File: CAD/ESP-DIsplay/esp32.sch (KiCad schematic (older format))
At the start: 7 parts, among them U401 ESP32-WROOM-32

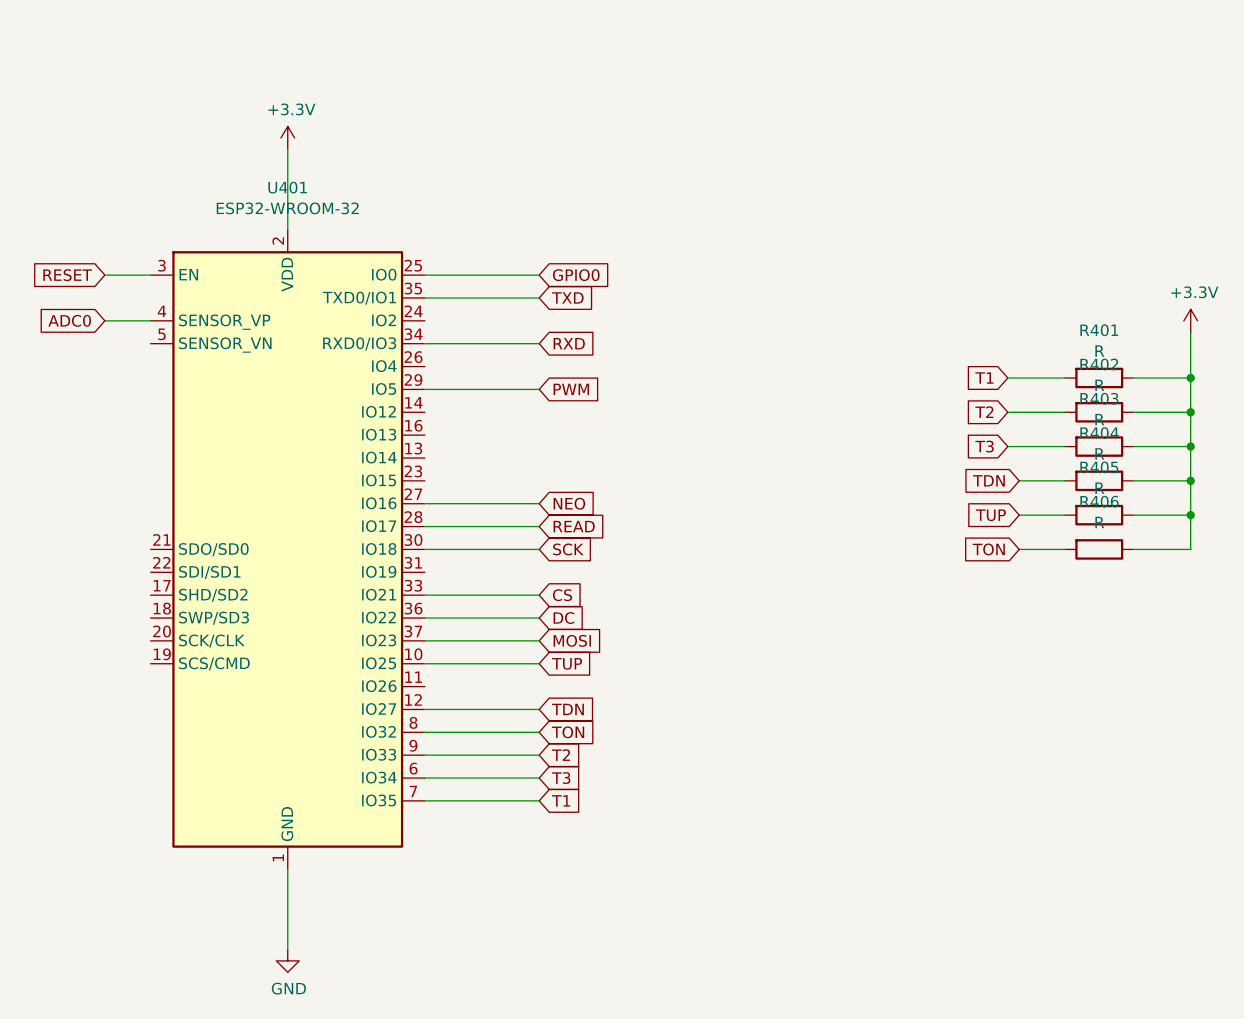
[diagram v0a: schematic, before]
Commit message: ESP Display v1
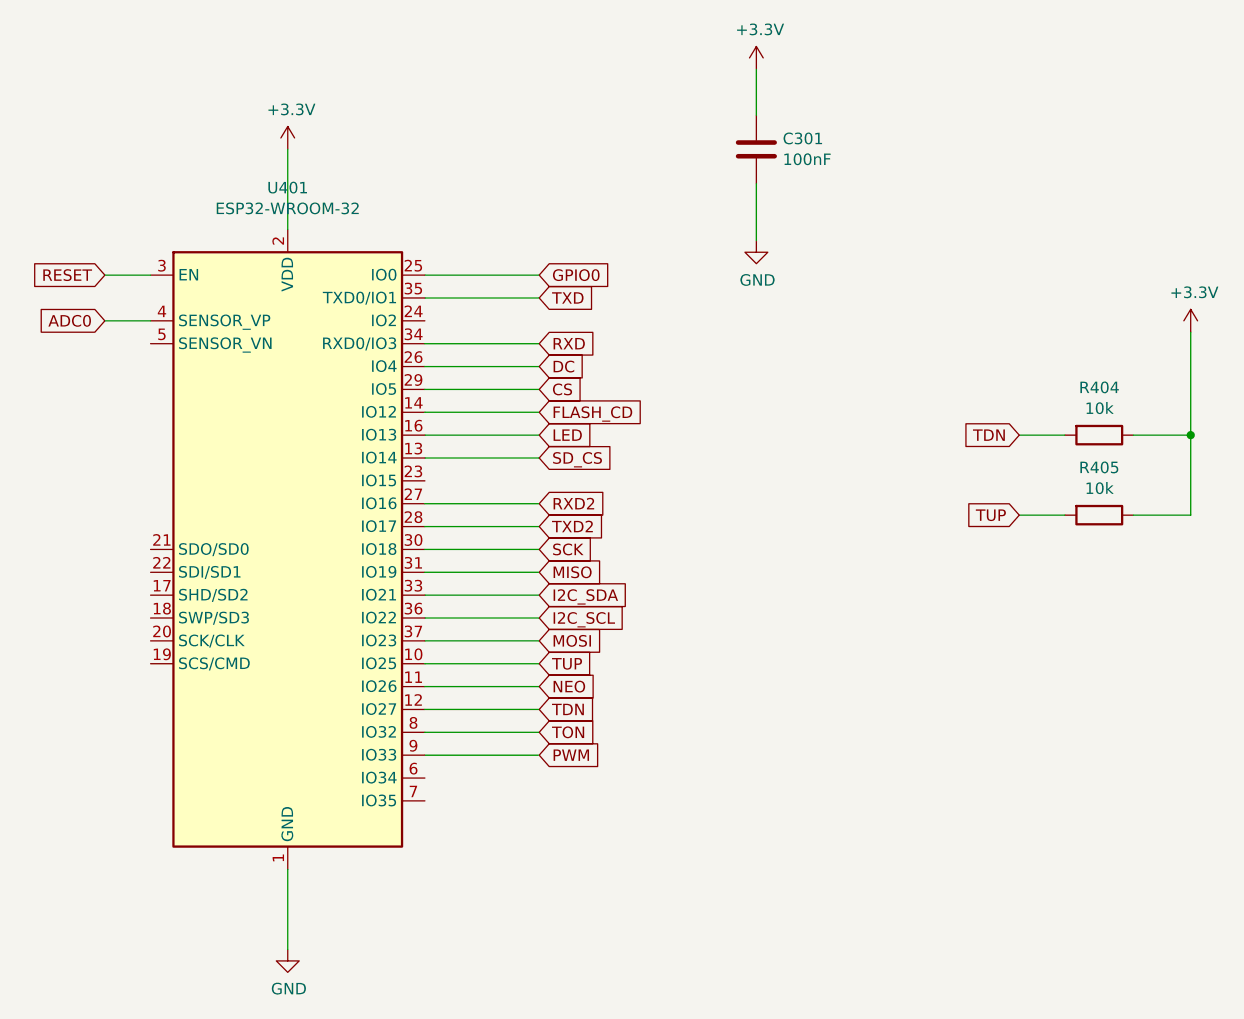
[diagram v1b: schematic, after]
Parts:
- removed R401, R402, R403, R406: R, Resistor_SMD:R_0805_2012Metric, symbol Device:R
- added C301: 100nF, Capacitor_SMD:C_1206_3216Metric, symbol Device:C
- R404, R405: value R -> 10k
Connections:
- net T2 is gone; now on net PWM: U401.9 (IO33)
- net +3V3: now also C301.1
- net CS: now also U401.29 (IO5); no longer U401.33 (IO21)
- net DC: now also U401.26 (IO4); no longer U401.36 (IO22)
- net GND: now also C301.2
- net NEO: now also U401.11 (IO26); no longer U401.27 (IO16)
- net PWM: no longer U401.29 (IO5)
- net SD_CS: now reaches U401.13 (IO14)
- net FLASH_CD: now reaches U401.14 (IO12)
- net LED: now reaches U401.16 (IO13)
- net MISO: now reaches U401.31 (IO19)
- net READ renamed TXD2
- net T1: no longer names the net of U401.7 (IO35)
- net T3: no longer names the net of U401.6 (IO34)
- new net I2C_SCL: U401.36 (IO22)
- new net I2C_SDA: U401.33 (IO21)
- new net RXD2: U401.27 (IO16)
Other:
- moved on the sheet: R404
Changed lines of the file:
@@
 $Descr A4 11693 8268
 encoding utf-8
-Sheet 4 9
+Sheet 3 8
 Title ""
 Date ""
@@
 Text GLabel 4450 2250 0    50   Input ~ 0
 RESET
-Text GLabel 8400 2700 0    50   Input ~ 0
-T1
-Text GLabel 8400 2850 0    50   Input ~ 0
-T2
-Text GLabel 8400 3000 0    50   Input ~ 0
-T3
-Text GLabel 8450 3150 0    50   Input ~ 0
+Text GLabel 8450 2950 0    50   Input ~ 0
 TDN
 Text GLabel 8450 3300 0    50   Input ~ 0
 TUP
-Text GLabel 8450 3450 0    50   Input ~ 0
-TON
-$Comp
-L Device:R R401
-U 1 1 609E9D28
-P 8800 2700
-F 0 "R401" V 8593 2700 50  0000 C CNN
-F 1 "R" V 8684 2700 50  0000 C CNN
-F 2 "Resistor_SMD:R_0805_2012Metric" V 8730 2700 50  0001 C CNN
-F 3 "~" H 8800 2700 50  0001 C CNN
-	1    8800 2700
-	0    1    1    0
-$EndComp
-$Comp
-L Device:R R402
-U 1 1 609E9DFD
-P 8800 2850
-F 0 "R402" V 8593 2850 50  0000 C CNN
-F 1 "R" V 8684 2850 50  0000 C CNN
-F 2 "Resistor_SMD:R_0805_2012Metric" V 8730 2850 50  0001 C CNN
-F 3 "~" H 8800 2850 50  0001 C CNN
-	1    8800 2850
-	0    1    1    0
-$EndComp
-$Comp
-L Device:R R403
-U 1 1 609EA1B1
-P 8800 3000
-F 0 "R403" V 8593 3000 50  0000 C CNN
-F 1 "R" V 8684 3000 50  0000 C CNN
-F 2 "Resistor_SMD:R_0805_2012Metric" V 8730 3000 50  0001 C CNN
-F 3 "~" H 8800 3000 50  0001 C CNN
-	1    8800 3000
-	0    1    1    0
-$EndComp
 $Comp
 L Device:R R404
 U 1 1 609EA50A
-P 8800 3150
-F 0 "R404" V 8593 3150 50  0000 C CNN
-F 1 "R" V 8684 3150 50  0000 C CNN
-F 2 "Resistor_SMD:R_0805_2012Metric" V 8730 3150 50  0001 C CNN
-F 3 "~" H 8800 3150 50  0001 C CNN
-	1    8800 3150
+P 8800 2950
+F 0 "R404" V 8593 2950 50  0000 C CNN
+F 1 "10k" V 8684 2950 50  0000 C CNN
+F 2 "Resistor_SMD:R_0805_2012Metric" V 8730 2950 50  0001 C CNN
+F 3 "~" H 8800 2950 50  0001 C CNN
+	1    8800 2950
 	0    1    1    0
 $EndComp
@@
 P 8800 3300
 F 0 "R405" V 8593 3300 50  0000 C CNN
-F 1 "R" V 8684 3300 50  0000 C CNN
+F 1 "10k" V 8684 3300 50  0000 C CNN
 F 2 "Resistor_SMD:R_0805_2012Metric" V 8730 3300 50  0001 C CNN
 F 3 "~" H 8800 3300 50  0001 C CNN
 	1    8800 3300
-	0    1    1    0
-$EndComp
-$Comp
-L Device:R R406
-U 1 1 609EAC1B
-P 8800 3450
-F 0 "R406" V 8593 3450 50  0000 C CNN
-F 1 "R" V 8684 3450 50  0000 C CNN
-F 2 "Resistor_SMD:R_0805_2012Metric" V 8730 3450 50  0001 C CNN
-F 3 "~" H 8800 3450 50  0001 C CNN
-	1    8800 3450
 	0    1    1    0
 $EndComp
@@
 $EndComp
 Wire Wire Line
-	8400 2700 8650 2700
-Wire Wire Line
-	8400 2850 8650 2850
-Wire Wire Line
-	8400 3000 8650 3000
-Wire Wire Line
-	8450 3150 8650 3150
+	8450 2950 8650 2950
 Wire Wire Line
 	8450 3300 8650 3300
 Wire Wire Line
-	8450 3450 8650 3450
-Wire Wire Line
-	8950 3450 9200 3450
-Wire Wire Line
-	9200 3450 9200 3300
-Wire Wire Line
-	8950 2700 9200 2700
-Connection ~ 9200 2700
-Wire Wire Line
-	9200 2700 9200 2500
-Wire Wire Line
-	8950 2850 9200 2850
-Connection ~ 9200 2850
-Wire Wire Line
-	9200 2850 9200 2700
-Wire Wire Line
-	8950 3000 9200 3000
-Connection ~ 9200 3000
-Wire Wire Line
-	9200 3000 9200 2850
-Wire Wire Line
-	8950 3150 9200 3150
-Connection ~ 9200 3150
-Wire Wire Line
-	9200 3150 9200 3000
+	8950 2950 9200 2950
 Wire Wire Line
 	8950 3300 9200 3300
-Connection ~ 9200 3300
-Wire Wire Line
-	9200 3300 9200 3150
-Text GLabel 6350 2750 2    50   Input ~ 0
+Text GLabel 6350 4350 2    50   Input ~ 0
 PWM
-Text GLabel 6350 3250 2    50   Input ~ 0
+Text GLabel 6350 4050 2    50   Input ~ 0
 NEO
-Text GLabel 6350 3350 2    50   Input ~ 0
-READ
 Text GLabel 6350 3450 2    50   Input ~ 0
 SCK
 Text GLabel 6350 4250 2    50   Input ~ 0
 TON
-Text GLabel 6350 4350 2    50   Input ~ 0
-T2
-Text GLabel 6350 4450 2    50   Input ~ 0
-T3
-Text GLabel 6350 4550 2    50   Input ~ 0
-T1
-Text GLabel 6350 3650 2    50   Input ~ 0
+Text GLabel 6350 2750 2    50   Input ~ 0
 CS
-Text GLabel 6350 3750 2    50   Input ~ 0
+Text GLabel 6350 2650 2    50   Input ~ 0
 DC
 Wire Wire Line
-	5850 2750 6350 2750
-Wire Wire Line
-	5850 3250 6350 3250
-Wire Wire Line
-	5850 3350 6350 3350
-Wire Wire Line
-	5850 3450 6350 3450
-Wire Wire Line
-	5850 3650 6350 3650
-Wire Wire Line
-	5850 3750 6350 3750
-Wire Wire Line
 	5850 4250 6350 4250
-Wire Wire Line
-	5850 4350 6350 4350
-Wire Wire Line
-	5850 4450 6350 4450
-Wire Wire Line
-	5850 4550 6350 4550
 Text GLabel 6350 3850 2    50   Input ~ 0
 MOSI
@@
 Text GLabel 4450 2450 0    50   Input ~ 0
 ADC0
+Wire Wire Line
+	5850 4050 6350 4050
+Text GLabel 6350 3250 2    50   Input ~ 0
+RXD2
+Text GLabel 6350 3350 2    50   Input ~ 0
+TXD2
+Wire Wire Line
+	5850 3450 6350 3450
+Wire Wire Line
+	5850 3250 6350 3250
+Wire Wire Line
+	5850 3350 6350 3350
+$Comp
+L Device:C C301
+U 1 1 608BFD52
+P 7300 1700
+F 0 "C301" H 7415 1746 50  0000 L CNN
+F 1 "100nF" H 7415 1655 50  0000 L CNN
+F 2 "Capacitor_SMD:C_1206_3216Metric" H 7338 1550 50  0001 C CNN
+F 3 "~" H 7300 1700 50  0001 C CNN
+	1    7300 1700
+	1    0    0    -1
+$EndComp
+$Comp
+L power:GND #PWR0130
+U 1 1 608C0BEA
+P 7300 2100
+F 0 "#PWR0130" H 7300 1850 50  0001 C CNN
+F 1 "GND" H 7305 1927 50  0000 C CNN
+F 2 "" H 7300 2100 50  0001 C CNN
+F 3 "" H 7300 2100 50  0001 C CNN
+	1    7300 2100
+	1    0    0    -1
+$EndComp
+$Comp
+L power:+3.3V #PWR0131
+U 1 1 608C0EEE
+P 7300 1350
+F 0 "#PWR0131" H 7300 1200 50  0001 C CNN
+F 1 "+3.3V" H 7315 1523 50  0000 C CNN
+F 2 "" H 7300 1350 50  0001 C CNN
+F 3 "" H 7300 1350 50  0001 C CNN
+	1    7300 1350
+	1    0    0    -1
+$EndComp
+Text GLabel 6350 2950 2    50   Input ~ 0
+LED
+Wire Wire Line
+	5850 2950 6350 2950
+Text GLabel 6350 3750 2    50   Input ~ 0
+I2C_SCL
+Text GLabel 6350 3650 2    50   Input ~ 0
+I2C_SDA
+Wire Wire Line
+	5850 3650 6350 3650
+Wire Wire Line
+	5850 3750 6350 3750
+Wire Wire Line
+	5850 2650 6350 2650
+Wire Wire Line
+	9200 2500 9200 2950
+Connection ~ 9200 2950
+Wire Wire Line
+	9200 2950 9200 3300
+Text GLabel 6350 3550 2    50   Input ~ 0
+MISO
+Wire Wire Line
+	5850 3550 6350 3550
+Wire Wire Line
+	5850 2750 6350 2750
+Wire Wire Line
+	5850 4350 6350 4350
+Wire Wire Line
+	7300 1850 7300 2100
+Wire Wire Line
+	7300 1350 7300 1550
+Text GLabel 6350 3050 2    50   Input ~ 0
+SD_CS
+Wire Wire Line
+	5850 3050 6350 3050
+Text GLabel 6350 2850 2    50   Input ~ 0
+FLASH_CD
+Wire Wire Line
+	5850 2850 6350 2850
 $EndSCHEMATC
